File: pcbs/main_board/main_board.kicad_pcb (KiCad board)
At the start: 2 copper layers, 70 x 61.3 mm, 56 parts, among them J1 BAT1, J2 BAT2, J3 LED strip, J4 Motor, Q1 NMOS, Q2 NMOS, SW1 Power switch, U1 mini_esp32, U10 LM74610QDGKRQ1, U11 LM74610QDGKRQ1, U2 ADXL345, U3 DRV8873HPWPRQ1, U4 Display, U5 Step-up, U6 TPS22917LDBV, U8 ST1L08, U9 TXU0101

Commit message: Main board final update
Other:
- board text added: "NOTES: - Rozměry PCB převzaty z modelu ve Fusionu - navrhl jsem umístění ESP, je potřeba ho umístit někam, kam se snadno vejde USB kabel, takže se klidně může přemístit, ale je třeba na to myslet - Když na to tak koukám, tak se vše pravděpodobně nevejde na jednu stranu, oboustrané PCB nevadí, jen by bylo vhodné dát na stranu FRONT konektory. - Co se týče konektorů obecně myslet na to, že za hrani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"
- board text removed: "NOTES: - Rozměry PCB převzaty z modelu ve Fusionu - navrhl jsem umístění ESP, je potřeba ho umístit někam, kam se snadno vejde USB kabel, takže se klidně může přemístit, ale je třeba na to myslet - Když na to tak koukám, tak se vše pravděpodobně nevejde na jednu stranu, oboustrané PCB nevadí, jen by bylo vhodné dát na stranu FRONT konektory. A podle modelu ve fusionu kouknout kam to na BOTTOM str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"
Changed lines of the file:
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@@
 		)
 	)
-	(gr_text "NOTES:\n- Rozměry PCB převzaty z modelu ve Fusionu\n- navrhl jsem umístění ESP, je potřeba ho umístit někam, kam se snadno vejde USB kabel, \n  takže se klidně může přemístit, ale je třeba na to myslet\n- Když na to tak koukám, tak se vše pravděpodobně nevejde na jednu stranu,\n  oboustrané PCB nevadí, jen by bylo vhodné dát na stranu FRONT konektory. A podle modelu\n  ve fusionu kouknout kam to na BOTTOM stranu dát.\n- Co se týče konektorů obecně myslet na to, že za hranicí desky už bude stěna. A kabel z té strany\n  nepůjde připojit. Vůbec bych se tedy nebál nechat stranu FRONT pouze konektorům (a ESP), \n  ať se tam konektory strkají lépe.\n- U konektoru na displej je potřeba ohlídat jeho orientaci, případně přečíslovat footprint. \n  Cílem je, aby se kabel od displeje nekřížil, ale šel pěkně rovně. (Konektor displeje se bude\n  nacházet na levé straně (označeno komentářem).\n- Co se šířky cest týče, tak velký proud (4 A) poteče jen BATERIE -- LED PÁSEK\n- Menší výřez z nějaké strany v PCB by mohl být praktický pro protažení kabelů od baterií, \n  LED pásku a motoru."
+	(gr_text "NOTES:\n- Rozměry PCB převzaty z modelu ve Fusionu\n- navrhl jsem umístění ESP, je potřeba ho umístit někam, kam se snadno vejde USB kabel, \n  takže se klidně může přemístit, ale je třeba na to myslet\n- Když na to tak koukám, tak se vše pravděpodobně nevejde na jednu stranu,\n  oboustrané PCB nevadí, jen by bylo vhodné dát na stranu FRONT konektory.\n- Co se týče konektorů obecně myslet na to, že za hranicí desky už bude stěna. A kabel z té strany\n  nepůjde připojit. Vůbec bych se tedy nebál nechat stranu FRONT pouze konektorům (a ESP), \n  ať se tam konektory strkají lépe.\n- U konektoru na displej je potřeba ohlídat jeho orientaci, případně přečíslovat footprint. \n  Cílem je, aby se kabel od displeje nekřížil, ale šel pěkně rovně. (Konektor displeje se bude\n  nacházet na levé straně (označeno komentářem).\n- Co se šířky cest týče, tak velký proud (4 A) poteče jen BATERIE -- LED PÁSEK\n- Menší výřez z nějaké strany v PCB by mohl být praktický pro protažení kabelů od baterií, \n  LED pásku a motoru."
 		(at 18.44 108.41 0)
 		(layer "Dwgs.User")

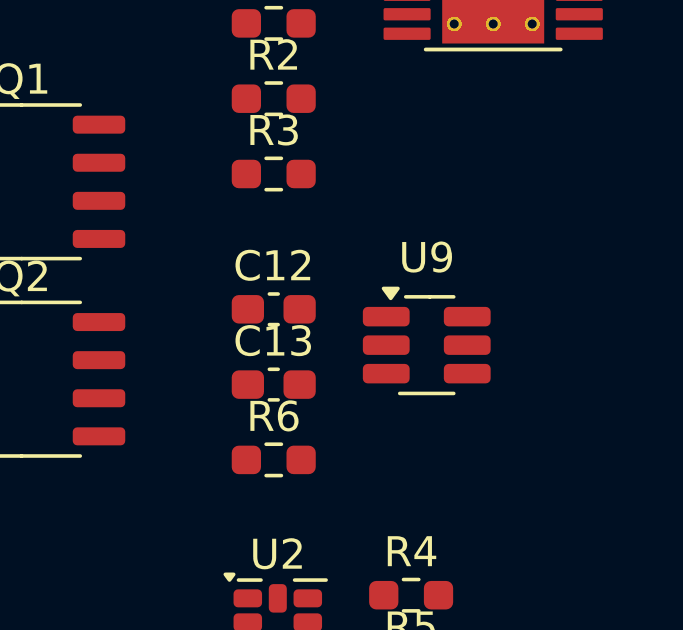
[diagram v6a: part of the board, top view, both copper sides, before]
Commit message: changed footprint of level shifter
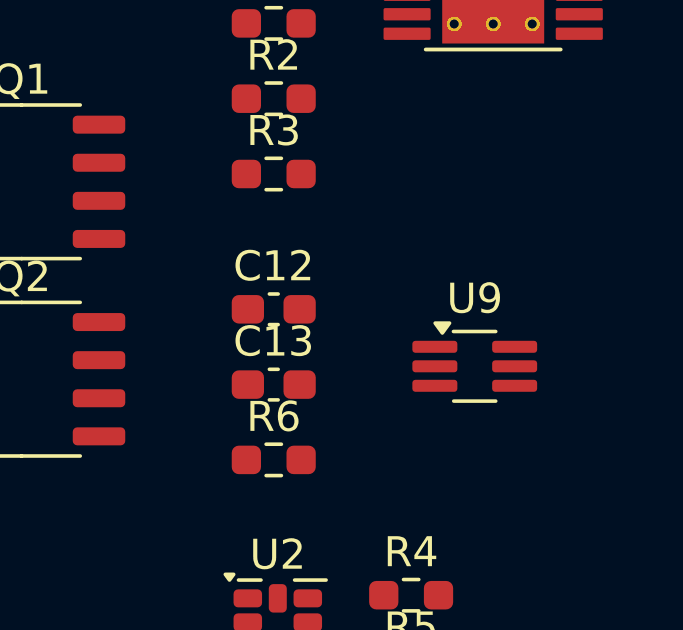
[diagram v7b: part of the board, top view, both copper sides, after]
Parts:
- U9: footprint Package_TO_SOT_SMD:SOT-23-6_Handsoldering -> Package_TO_SOT_SMD:SOT-363_SC-70-6_Handsoldering
- moved U9 1.75 mm to (171.5, 49.9)
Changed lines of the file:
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@@
 		)
 	)
-	(footprint "Package_TO_SOT_SMD:SOT-23-6_Handsoldering"
+	(footprint "Package_TO_SOT_SMD:SOT-363_SC-70-6_Handsoldering"
 		(layer "F.Cu")
-		(at 169.94 49.175)
-		(descr "6-pin SOT-23 package, Handsoldering")
-		(tags "SOT-23-6 Handsoldering")
+		(at 171.54 49.88)
+		(descr "SOT-363, SC-70-6, SC-88, Handsoldering")
+		(tags "SOT-363 SC-70-6 SC-88 Handsoldering")
 		(property "Reference" "U9"
-			(at 0 -2.9 0)
+			(at 0 -2.25 0)
 			(layer "F.SilkS")
 			(effects
@@
 		)
 		(property "Value" "TXU0101"
-			(at 0 2.9 0)
+			(at 0 2 180)
 			(layer "F.Fab")
 			(effects
@@
 			)
 		)
-		(property "Manufacturer Part Number" "TXU0101DBVR"
+		(property "Manufacturer Part Number" "TXU0101DCKR"
 			(at 0 0 0)
 			(unlocked yes)
@@
 			)
 		)
-		(property "Supplier Part Number" "595-TXU0101DBVR"
-			(at 0 0 0)
-			(unlocked yes)
-			(layer "F.Fab")
-			(hide yes)
-			(effects
-				(font
-					(size 1 1)
-					(thickness 0.15)
-				)
-			)
-		)
-		(property "Mouser number" ""
+		(property "Supplier Part Number" "595-TXU0101DCKR"
 			(at 0 0 0)
 			(unlocked yes)
@@
 		(attr smd)
 		(fp_line
-			(start -0.9 1.61)
-			(end 0.9 1.61)
+			(start -0.71 -1.16)
+			(end 0.7 -1.16)
 			(stroke
 				(width 0.12)
@@
 		)
 		(fp_line
-			(start 0.1 -1.61)
-			(end -0.7 -1.61)
-			(stroke
-				(width 0.12)
-				(type solid)
-			)
-			(layer "F.SilkS")
-		)
-		(fp_line
-			(start 0.1 -1.61)
-			(end 0.9 -1.61)
+			(start -0.7 1.16)
+			(end 0.7 1.16)
 			(stroke
 				(width 0.12)
@@
 		(fp_poly
 			(pts
-				(xy -1.2 -1.56) (xy -1.44 -1.89) (xy -0.96 -1.89) (xy -1.2 -1.56)
+				(xy -1.08 -1.11) (xy -1.32 -1.44) (xy -0.84 -1.44) (xy -1.08 -1.11)
 			)
 			(stroke
@@
 		)
 		(fp_line
-			(start -2.4 -1.8)
-			(end 2.4 -1.8)
-			(stroke
-				(width 0.05)
-				(type solid)
-			)
-			(layer "F.CrtYd")
-		)
-		(fp_line
-			(start -2.4 1.8)
-			(end -2.4 -1.8)
-			(stroke
-				(width 0.05)
-				(type solid)
-			)
-			(layer "F.CrtYd")
-		)
-		(fp_line
-			(start 2.4 -1.8)
-			(end 2.4 1.8)
-			(stroke
-				(width 0.05)
-				(type solid)
-			)
-			(layer "F.CrtYd")
-		)
-		(fp_line
-			(start 2.4 1.8)
-			(end -2.4 1.8)
-			(stroke
-				(width 0.05)
-				(type solid)
-			)
-			(layer "F.CrtYd")
-		)
-		(fp_line
-			(start -0.9 -0.9)
-			(end -0.9 1.55)
-			(stroke
-				(width 0.1)
-				(type solid)
-			)
-			(layer "F.Fab")
-		)
-		(fp_line
-			(start -0.9 -0.9)
-			(end -0.25 -1.55)
-			(stroke
-				(width 0.1)
-				(type solid)
-			)
-			(layer "F.Fab")
-		)
-		(fp_line
-			(start 0.9 -1.55)
-			(end -0.25 -1.55)
-			(stroke
-				(width 0.1)
-				(type solid)
-			)
-			(layer "F.Fab")
-		)
-		(fp_line
-			(start 0.9 -1.55)
-			(end 0.9 1.55)
-			(stroke
-				(width 0.1)
-				(type solid)
-			)
-			(layer "F.Fab")
-		)
-		(fp_line
-			(start 0.9 1.55)
-			(end -0.9 1.55)
+			(start -2.4 -1.4)
+			(end -2.4 1.4)
+			(stroke
+				(width 0.05)
+				(type solid)
+			)
+			(layer "F.CrtYd")
+		)
+		(fp_line
+			(start -2.4 -1.4)
+			(end 2.4 -1.4)
+			(stroke
+				(width 0.05)
+				(type solid)
+			)
+			(layer "F.CrtYd")
+		)
+		(fp_line
+			(start -2.4 1.4)
+			(end 2.4 1.4)
+			(stroke
+				(width 0.05)
+				(type solid)
+			)
+			(layer "F.CrtYd")
+		)
+		(fp_line
+			(start 2.4 1.4)
+			(end 2.4 -1.4)
+			(stroke
+				(width 0.05)
+				(type solid)
+			)
+			(layer "F.CrtYd")
+		)
+		(fp_line
+			(start -0.675 -0.6)
+			(end -0.675 1.1)
+			(stroke
+				(width 0.1)
+				(type solid)
+			)
+			(layer "F.Fab")
+		)
+		(fp_line
+			(start -0.175 -1.1)
+			(end -0.675 -0.6)
+			(stroke
+				(width 0.1)
+				(type solid)
+			)
+			(layer "F.Fab")
+		)
+		(fp_line
+			(start 0.675 -1.1)
+			(end -0.175 -1.1)
+			(stroke
+				(width 0.1)
+				(type solid)
+			)
+			(layer "F.Fab")
+		)
+		(fp_line
+			(start 0.675 -1.1)
+			(end 0.675 1.1)
+			(stroke
+				(width 0.1)
+				(type solid)
+			)
+			(layer "F.Fab")
+		)
+		(fp_line
+			(start 0.675 1.1)
+			(end -0.675 1.1)
 			(stroke
 				(width 0.1)
@@
 		)
 		(pad "1" smd roundrect
-			(at -1.35 -0.95)
-			(size 1.56 0.65)
+			(at -1.33 -0.65)
+			(size 1.5 0.4)
 			(layers "F.Cu" "F.Mask" "F.Paste")
 			(roundrect_rratio 0.25)
@@
 		)
 		(pad "2" smd roundrect
-			(at -1.35 0)
-			(size 1.56 0.65)
+			(at -1.33 0)
+			(size 1.5 0.4)
 			(layers "F.Cu" "F.Mask" "F.Paste")
 			(roundrect_rratio 0.25)
@@
 		)
 		(pad "3" smd roundrect
-			(at -1.35 0.95)
-			(size 1.56 0.65)
+			(at -1.33 0.65)
+			(size 1.5 0.4)
 			(layers "F.Cu" "F.Mask" "F.Paste")
 			(roundrect_rratio 0.25)
@@
 		)
 		(pad "4" smd roundrect
-			(at 1.35 0.95)
-			(size 1.56 0.65)
+			(at 1.33 0.65)
+			(size 1.5 0.4)
 			(layers "F.Cu" "F.Mask" "F.Paste")
 			(roundrect_rratio 0.25)
@@
 		)
 		(pad "5" smd roundrect
-			(at 1.35 0)
-			(size 1.56 0.65)
+			(at 1.33 0)
+			(size 1.5 0.4)
 			(layers "F.Cu" "F.Mask" "F.Paste")
 			(roundrect_rratio 0.25)
@@
 		)
 		(pad "6" smd roundrect
-			(at 1.35 -0.95)
-			(size 1.56 0.65)
+			(at 1.33 -0.65)
+			(size 1.5 0.4)
 			(layers "F.Cu" "F.Mask" "F.Paste")
 			(roundrect_rratio 0.25)
@@
 		)
 		(embedded_fonts no)
-		(model "${KICAD9_3DMODEL_DIR}/Package_TO_SOT_SMD.3dshapes/SOT-23-6.step"
+		(model "${KICAD9_3DMODEL_DIR}/Package_TO_SOT_SMD.3dshapes/SOT-363_SC-70-6.step"
 			(offset
 				(xyz 0 0 0)

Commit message: Main board layout design
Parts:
- C1, C10, C11, C12, C13, C14, C15, C16, C17, C2, C3, C4, C5, C6, C7, F1, GND2, Q1, Q2, R1, R10, R11, R12, R13, R16, R2, R3, R4, R5, R6, R7, R8, R9, U10, U11, U2, U3, U5, U6, U8, U9: moved to B.Cu
- moved C5 116.8 mm to (58.6, 54.7)
- moved C3 115.4 mm to (51.2, 51.2), turned to 180 degrees
- moved U3 115.2 mm to (57.6, 47.2), turned to 180 degrees
- moved C2 115.2 mm to (51.1, 46.3), turned to 180 degrees
- moved C4 114.7 mm to (51.1, 48.0), turned to 180 degrees
- moved C1 114.2 mm to (52.0, 43.6), turned to 90 degrees
- moved U9 111.3 mm to (63.4, 76.4)
- moved C12 109.1 mm to (59.9, 78.0), turned to -90 degrees
- moved U5 107.6 mm to (38.6, 69.7), turned to 90 degrees
- moved U2 105.2 mm to (62.9, 34.2), turned to 180 degrees
- moved C6 104.5 mm to (60.5, 41.1), turned to 90 degrees
- moved R2 102.2 mm to (62.6, 41.0), turned to 90 degrees
- moved R6 100.1 mm to (67.8, 77.6), turned to 90 degrees
- moved C13 99.9 mm to (67.8, 73.9), turned to 90 degrees
- moved SW1 97.4 mm to (57.0, 84.2), turned to -90 degrees
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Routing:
- net GND: track 0.00 -> 352.2 mm, vias 0 -> 34
- net +3.3V: track 0.00 -> 130.7 mm, vias 0 -> 3
- net +VBAT: track 0.00 -> 85.7 mm, vias 0 -> 1
- net /B_STATUS: track 0.00 -> 60.5 mm, vias 0 -> 2
- net /Display/DC/RS: track 0.00 -> 48.1 mm, vias 0 -> 1
- net Net-(SW1A-A): track 0.00 -> 47.8 mm
- net /Display/RESET: track 0.00 -> 45.7 mm
- net /M_IPROP: track 0.00 -> 44.5 mm
- net /Display/MOSI: track 0.00 -> 44.3 mm
- net /Display/SCK: track 0.00 -> 44.3 mm
- net /Display/CS: track 0.00 -> 43.3 mm
- net +5V: track 0.00 -> 37.3 mm, vias 0 -> 2
- net /DC motor driver/MOTOR1: track 0.00 -> 34.7 mm, vias 0 -> 2
- net /Accelerometer/SDA: track 0.00 -> 33.2 mm, vias 0 -> 2
- net /Accelerometer/SCL: track 0.00 -> 32.6 mm, vias 0 -> 1
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- added copper zone on B.Cu, net (none)
- added copper zone on F.Cu, net (none)
- added copper zone on B.Cu, net GND
- added copper zone on F.Cu, net GND
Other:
- board size 70 x 61.3 mm -> 70 x 61.2 mm
